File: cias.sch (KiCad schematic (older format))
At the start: 63 parts, among them CN13 KEYBOARD, CN6 SERIAL_DB25M, CN7 PARALLEL_DB25F, Q501 2N3904, Q502 2N3906, Q503 2N3906, Q711 2N3904, U38 MC1488, U39 MC1489, U42 NE555, U7 VIA_8520, U8 VIA_8520

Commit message: Almost all components positioned
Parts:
- C502: footprint (none) -> Raemixx500:C_Axial_L9.0mm_D3.2mm_P12.70mm
- E532, E533, E534, E535, E536, E537, E631, E632: footprint (none) -> Raemixx500:EMI_Filter_Short
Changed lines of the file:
@@
 F 0 "E532" H 7905 6900 50  0000 C CNN
 F 1 "150p" H 7855 6680 50  0000 C CNN
-F 2 "" V 8045 6710 50  0001 C CNN
+F 2 "Raemixx500:EMI_Filter_Short" V 8045 6710 50  0001 C CNN
 F 3 "http://www.murata.com/~/media/webrenewal/support/library/catalog/products/emc/emifil/c31e.ashx?la=en-gb" V 8045 6710 50  0001 C CNN
 	1    8045 6710
@@
 F 0 "E534" H 8430 7105 50  0000 C CNN
 F 1 "150p" H 8595 6880 50  0000 C CNN
-F 2 "" V 8430 6910 50  0001 C CNN
+F 2 "Raemixx500:EMI_Filter_Short" V 8430 6910 50  0001 C CNN
 F 3 "http://www.murata.com/~/media/webrenewal/support/library/catalog/products/emc/emifil/c31e.ashx?la=en-gb" V 8430 6910 50  0001 C CNN
 	1    8430 6910
@@
 F 0 "E533" H 7905 7300 50  0000 C CNN
 F 1 "470p" H 7855 7085 50  0000 C CNN
-F 2 "" V 8045 7110 50  0001 C CNN
+F 2 "Raemixx500:EMI_Filter_Short" V 8045 7110 50  0001 C CNN
 F 3 "http://www.murata.com/~/media/webrenewal/support/library/catalog/products/emc/emifil/c31e.ashx?la=en-gb" V 8045 7110 50  0001 C CNN
 	1    8045 7110
@@
 F 0 "E535" H 8430 7505 50  0000 C CNN
 F 1 "470p" H 8600 7280 50  0000 C CNN
-F 2 "" V 8430 7310 50  0001 C CNN
+F 2 "Raemixx500:EMI_Filter_Short" V 8430 7310 50  0001 C CNN
 F 3 "http://www.murata.com/~/media/webrenewal/support/library/catalog/products/emc/emifil/c31e.ashx?la=en-gb" V 8430 7310 50  0001 C CNN
 	1    8430 7310
@@
 F 0 "E536" H 7905 7700 50  0000 C CNN
 F 1 "470p" H 7860 7480 50  0000 C CNN
-F 2 "" V 8045 7510 50  0001 C CNN
+F 2 "Raemixx500:EMI_Filter_Short" V 8045 7510 50  0001 C CNN
 F 3 "http://www.murata.com/~/media/webrenewal/support/library/catalog/products/emc/emifil/c31e.ashx?la=en-gb" V 8045 7510 50  0001 C CNN
 	1    8045 7510
@@
 F 0 "E537" H 7905 8100 50  0000 C CNN
 F 1 "470p" H 7860 7880 50  0000 C CNN
-F 2 "" V 8045 7910 50  0001 C CNN
+F 2 "Raemixx500:EMI_Filter_Short" V 8045 7910 50  0001 C CNN
 F 3 "http://www.murata.com/~/media/webrenewal/support/library/catalog/products/emc/emifil/c31e.ashx?la=en-gb" V 8045 7910 50  0001 C CNN
 	1    8045 7910
@@
 F 0 "C502" V 8570 8410 50  0000 C CNN
 F 1 "330n" V 8415 8280 50  0000 C CNN
-F 2 "" H 8460 8410 50  0001 C CNN
+F 2 "Raemixx500:C_Axial_L9.0mm_D3.2mm_P12.70mm" H 8460 8410 50  0001 C CNN
 F 3 "~" H 8460 8410 50  0001 C CNN
 	1    8460 8410
@@
 F 0 "E632" H 14545 4275 50  0000 C CNN
 F 1 "100p" H 14350 4055 50  0000 C CNN
-F 2 "" V 14545 4085 50  0001 C CNN
+F 2 "Raemixx500:EMI_Filter_Short" V 14545 4085 50  0001 C CNN
 F 3 "http://www.murata.com/~/media/webrenewal/support/library/catalog/products/emc/emifil/c31e.ashx?la=en-gb" V 14545 4085 50  0001 C CNN
 	1    14545 4085
@@
 F 0 "E631" H 14545 4630 50  0000 C CNN
 F 1 "100p" H 14350 4410 50  0000 C CNN
-F 2 "" V 14545 4440 50  0001 C CNN
+F 2 "Raemixx500:EMI_Filter_Short" V 14545 4440 50  0001 C CNN
 F 3 "http://www.murata.com/~/media/webrenewal/support/library/catalog/products/emc/emifil/c31e.ashx?la=en-gb" V 14545 4440 50  0001 C CNN
 	1    14545 4440

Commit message: Work in progress
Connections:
- net GND: now also E531.2, E538.2
- net at E535.1: now also U39.4 (IN_B); no longer U39.13 (IN_D)
- net at E536.1: now also U39.10 (IN_C); no longer U39.4 (IN_B)
- net at E537.1: now also U39.13 (IN_D); no longer U39.10 (IN_C)
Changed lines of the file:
@@
 Wire Wire Line
 	8955 7410 8345 7410
-$Comp
-L emi_filter_lcl_small:EMI_Filter_LCL E536
-U 1 1 5EC70AF7
-P 8045 7510
-F 0 "E536" H 7905 7700 50  0000 C CNN
-F 1 "470p" H 7860 7480 50  0000 C CNN
-F 2 "Raemixx500:EMI_Filter_Short" V 8045 7510 50  0001 C CNN
-F 3 "http://www.murata.com/~/media/webrenewal/support/library/catalog/products/emc/emifil/c31e.ashx?la=en-gb" V 8045 7510 50  0001 C CNN
-	1    8045 7510
-	1    0    0    -1
-$EndComp
 Wire Wire Line
 	8955 7810 8345 7810
@@
 Wire Wire Line
 	5780 7060 6950 7060
-Wire Wire Line
-	5885 7210 8130 7210
 NoConn ~ 6090 7310
-Wire Wire Line
-	5885 7810 7745 7810
 NoConn ~ 5585 7710
 Wire Wire Line
@@
 Wire Wire Line
 	4980 5875 4065 5875
-Wire Wire Line
-	6390 7410 7745 7410
 Wire Wire Line
 	5890 7410 5080 7410
@@
 Wire Wire Line
 	13385 7495 13215 7495
+$Comp
+L emi_filter_lcl_small:EMI_Filter_LCL E536
+U 1 1 5EC70AF7
+P 8045 7510
+F 0 "E536" H 7905 7700 50  0000 C CNN
+F 1 "470p" H 7860 7480 50  0000 C CNN
+F 2 "Raemixx500:EMI_Filter_Short" V 8045 7510 50  0001 C CNN
+F 3 "http://www.murata.com/~/media/webrenewal/support/library/catalog/products/emc/emifil/c31e.ashx?la=en-gb" V 8045 7510 50  0001 C CNN
+	1    8045 7510
+	1    0    0    -1
+$EndComp
+Wire Wire Line
+	7040 7210 7040 7410
+Wire Wire Line
+	7040 7210 8130 7210
+Wire Wire Line
+	6820 7810 7745 7810
+Wire Wire Line
+	5885 7210 6820 7210
+Wire Wire Line
+	6820 7210 6820 7810
+Wire Wire Line
+	5885 7810 6545 7810
+Wire Wire Line
+	6390 7410 7040 7410
+Wire Wire Line
+	7745 7410 7235 7410
+Wire Wire Line
+	7235 7410 7235 7585
+Wire Wire Line
+	7235 7585 6545 7585
+Wire Wire Line
+	6545 7585 6545 7810
+$Comp
+L power:GND #PWR?
+U 1 1 5DBE430E
+P 10690 8395
+F 0 "#PWR?" H 10690 8145 50  0001 C CNN
+F 1 "GND" H 10695 8222 50  0000 C CNN
+F 2 "" H 10690 8395 50  0001 C CNN
+F 3 "" H 10690 8395 50  0001 C CNN
+	1    10690 8395
+	1    0    0    -1
+$EndComp
+Wire Wire Line
+	10690 8395 10690 8310
+Connection ~ 10690 8310
 Wire Bus Line
 	1785 3110 1785 6275

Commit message: Work in progress
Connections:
- net ~OVL renamed OVL
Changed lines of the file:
@@
 ~LED
 Text GLabel 4385 3310 2    50   Output ~ 0
-~OVL
+OVL
 $Comp
 L power:VCC #PWR0162
@@
 	6545 7585 6545 7810
 $Comp
-L power:GND #PWR?
+L power:GND #PWR0268
 U 1 1 5DBE430E
 P 10690 8395
-F 0 "#PWR?" H 10690 8145 50  0001 C CNN
+F 0 "#PWR0268" H 10690 8145 50  0001 C CNN
 F 1 "GND" H 10695 8222 50  0000 C CNN
 F 2 "" H 10690 8395 50  0001 C CNN

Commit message: Work in progress
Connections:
- net FIRE0 renamed ~FIRE0
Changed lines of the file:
@@
 ~FIRE1
 Text GLabel 4310 2710 2    50   Input ~ 0
-FIRE0
+~FIRE0
 Text GLabel 4580 2810 2    50   Input ~ 0
 ~RDY

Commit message: Work in progress
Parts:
- removed E501, E502, E503: 47, Raemixx500:EMI_Filter_Longer, symbol Device:R
- added E501, E502, E503: 47 1/2W, Raemixx500:EMI_Filter_Longer, symbol emi_filter_lcl_small:EMI_Filter_LCL
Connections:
- net +12V: now also E502.1
- net +v: now also E502.3
- net -12V: now also E503.1
- net -v: now also E503.3
- net GND: now also E501.2, E502.2, E503.2
- net VCC: now also E501.1
- net ~auto: now also E501.3
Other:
- note removed: "1/2W"
- moved on the sheet: C502
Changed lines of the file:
@@
 Sheet 6 14
 Title "Rämixx500"
-Date "2019-05-08"
+Date "2019-05-11"
 Rev "1git"
 Comp "SukkoPera"
@@
 Wire Wire Line
 	9555 1490 9805 1490
-$Comp
-L power:VCC #PWR0160
-U 1 1 5E872212
-P 10215 1425
-F 0 "#PWR0160" H 10215 1275 50  0001 C CNN
-F 1 "VCC" H 10232 1598 50  0000 C CNN
-F 2 "" H 10215 1425 50  0001 C CNN
-F 3 "" H 10215 1425 50  0001 C CNN
-	1    10215 1425
-	1    0    0    -1
-$EndComp
-Wire Wire Line
-	10215 1425 10215 1490
-Wire Wire Line
-	10215 1490 10105 1490
-$Comp
-L Device:R E501
-U 1 1 5E870508
-P 9955 1490
-F 0 "E501" V 9870 1490 50  0000 C CNN
-F 1 "47" V 9955 1490 50  0000 C CNN
-F 2 "Raemixx500:EMI_Filter_Longer" V 9885 1490 50  0001 C CNN
-F 3 "~" H 9955 1490 50  0001 C CNN
-	1    9955 1490
-	0    1    1    0
-$EndComp
-Text Notes 9845 1345 0    50   ~ 0
-1/2W
 Text Label 9590 1490 0    50   ~ 0
 ~auto
@@
 	9555 1890 9650 1890
 Wire Wire Line
-	10250 1890 10390 1890
-Text GLabel 10390 1890 2    50   Input ~ 0
+	10250 1890 10495 1890
+Text GLabel 10495 1890 2    50   Input ~ 0
 ~IORESET
 Connection ~ 9950 2090
@@
 	8780 9235 8780 9115
 Wire Wire Line
-	8780 7610 8780 9115
-Wire Wire Line
 	8430 7610 8780 7610
 Wire Wire Line
@@
 fg
 NoConn ~ 8560 6410
-$Comp
-L Device:R E503
-U 1 1 5EDCA2BC
-P 8505 8210
-F 0 "E503" V 8420 8210 50  0000 C CNN
-F 1 "47" V 8505 8210 50  0000 C CNN
-F 2 "Raemixx500:EMI_Filter_Longer" V 8435 8210 50  0001 C CNN
-F 3 "~" H 8505 8210 50  0001 C CNN
-	1    8505 8210
-	0    1    1    0
-$EndComp
-Text Notes 8180 8300 0    50   ~ 0
-1/2W
-$Comp
-L Device:R E502
-U 1 1 5EDDB02D
-P 8505 8010
-F 0 "E502" V 8420 8010 50  0000 C CNN
-F 1 "47" V 8505 8010 50  0000 C CNN
-F 2 "Raemixx500:EMI_Filter_Longer" V 8435 8010 50  0001 C CNN
-F 3 "~" H 8505 8010 50  0001 C CNN
-	1    8505 8010
-	0    1    1    0
-$EndComp
-Text Notes 8185 8095 0    50   ~ 0
-1/2W
-Wire Wire Line
-	8655 8010 8955 8010
-Wire Wire Line
-	8655 8210 8955 8210
 Wire Wire Line
 	7495 8010 7495 7990
 Wire Wire Line
-	7495 8010 8355 8010
+	7495 8010 8130 8010
 $Comp
 L power:+12V #PWR0164
@@
 	7495 8210 7495 8170
 Wire Wire Line
-	7495 8210 8355 8210
+	7495 8210 7745 8210
 Wire Wire Line
 	8560 8610 8955 8610
@@
 Text GLabel 10355 7310 2    50   Output ~ 0
 AUDIN
-Wire Wire Line
-	8955 8410 8560 8410
 $Comp
 L Device:C_Small C502
 U 1 1 5EEC226F
-P 8460 8410
-F 0 "C502" V 8570 8410 50  0000 C CNN
-F 1 "330n" V 8415 8280 50  0000 C CNN
-F 2 "Raemixx500:C_Axial_L9.0mm_D3.2mm_P12.70mm" H 8460 8410 50  0001 C CNN
-F 3 "~" H 8460 8410 50  0001 C CNN
-	1    8460 8410
+P 7935 8610
+F 0 "C502" V 8045 8610 50  0000 C CNN
+F 1 "330n" V 7890 8480 50  0000 C CNN
+F 2 "Raemixx500:C_Axial_L9.0mm_D3.2mm_P12.70mm" H 7935 8610 50  0001 C CNN
+F 3 "~" H 7935 8610 50  0001 C CNN
+	1    7935 8610
 	0    1    1    0
 $EndComp
 Wire Wire Line
-	8360 8410 8155 8410
-Text GLabel 8155 8410 0    50   Input ~ 0
+	7835 8610 7390 8610
+Text GLabel 7390 8610 0    50   Input ~ 0
 AUDOUT
 Wire Wire Line
@@
 Wire Wire Line
 	5175 5675 4065 5675
-Text Notes 7240 8735 2    315  ~ 0
+Text Notes 7270 9190 2    315  ~ 0
 RS232
 Text Notes 8525 1090 2    315  ~ 0
@@
 Connection ~ 7615 8080
 Wire Wire Line
-	7615 8080 7615 9115
+	7615 8080 7615 8480
 $Comp
 L Device:R R713
@@
 	10690 8395 10690 8310
 Connection ~ 10690 8310
+$Comp
+L emi_filter_lcl_small:EMI_Filter_LCL E502
+U 1 1 5E0EA71F
+P 8430 8110
+F 0 "E502" H 8430 8305 50  0000 C CNN
+F 1 "47 1/2W" H 8600 8080 50  0000 C CNN
+F 2 "Raemixx500:EMI_Filter_Longer" V 8430 8110 50  0001 C CNN
+F 3 "http://www.murata.com/~/media/webrenewal/support/library/catalog/products/emc/emifil/c31e.ashx?la=en-gb" V 8430 8110 50  0001 C CNN
+	1    8430 8110
+	1    0    0    -1
+$EndComp
+$Comp
+L emi_filter_lcl_small:EMI_Filter_LCL E503
+U 1 1 5E0EA729
+P 8045 8310
+F 0 "E503" H 7905 8500 50  0000 C CNN
+F 1 "47 1/2W" H 7800 8280 50  0000 C CNN
+F 2 "Raemixx500:EMI_Filter_Longer" V 8045 8310 50  0001 C CNN
+F 3 "http://www.murata.com/~/media/webrenewal/support/library/catalog/products/emc/emifil/c31e.ashx?la=en-gb" V 8045 8310 50  0001 C CNN
+	1    8045 8310
+	1    0    0    -1
+$EndComp
+Wire Wire Line
+	8730 8010 8955 8010
+Wire Wire Line
+	8345 8210 8955 8210
+Wire Wire Line
+	8780 7610 8780 8270
+Wire Wire Line
+	8430 8160 8430 8270
+Wire Wire Line
+	8430 8270 8780 8270
+Connection ~ 8780 8270
+Wire Wire Line
+	8780 8270 8780 9115
+Wire Wire Line
+	8045 8360 8045 8480
+Wire Wire Line
+	8045 8480 7615 8480
+Connection ~ 7615 8480
+Wire Wire Line
+	7615 8480 7615 9115
+Wire Wire Line
+	8035 8610 8430 8610
+Wire Wire Line
+	8430 8610 8430 8410
+Wire Wire Line
+	8430 8410 8955 8410
+$Comp
+L power:VCC #PWR0160
+U 1 1 5E872212
+P 10515 1425
+F 0 "#PWR0160" H 10515 1275 50  0001 C CNN
+F 1 "VCC" H 10532 1598 50  0000 C CNN
+F 2 "" H 10515 1425 50  0001 C CNN
+F 3 "" H 10515 1425 50  0001 C CNN
+	1    10515 1425
+	1    0    0    -1
+$EndComp
+Wire Wire Line
+	10515 1425 10515 1490
+Wire Wire Line
+	10515 1490 10405 1490
+$Comp
+L emi_filter_lcl_small:EMI_Filter_LCL E501
+U 1 1 5E3D78DB
+P 10105 1590
+F 0 "E501" H 10105 1785 50  0000 C CNN
+F 1 "47 1/2W" H 9870 1560 50  0000 C CNN
+F 2 "Raemixx500:EMI_Filter_Longer" V 10105 1590 50  0001 C CNN
+F 3 "http://www.murata.com/~/media/webrenewal/support/library/catalog/products/emc/emifil/c31e.ashx?la=en-gb" V 10105 1590 50  0001 C CNN
+	1    10105 1590
+	-1   0    0    -1
+$EndComp
+Wire Wire Line
+	10105 1640 10105 1720
+Wire Wire Line
+	10105 1720 10325 1720
+Wire Wire Line
+	10325 1720 10325 2290
+Wire Wire Line
+	10325 2290 9950 2290
 Wire Bus Line
 	1785 3110 1785 6275

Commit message: Almost there :)
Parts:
- CN7: footprint w_conn_d-sub:DB_25M -> Raemixx500:DB_25F
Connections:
- net d0: no longer U8.33 (D0)
- net d1: no longer U8.32 (D1)
- net d2: no longer U8.31 (D2)
- net d3: no longer U8.30 (D3)
- net d4: no longer U8.29 (D4)
- net d5: no longer U8.28 (D5)
- net d6: no longer U8.27 (D6)
- net d7: no longer U8.26 (D7)
- new net d10: U8.31 (D2)
- new net d11: U8.30 (D3)
- new net d12: U8.29 (D4)
- new net d13: U8.28 (D5)
- new net d14: U8.27 (D6)
- new net d15: U8.26 (D7)
- new net d8: U8.33 (D0)
- new net d9: U8.32 (D1)
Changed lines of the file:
@@
 Sheet 6 14
 Title "Rämixx500"
-Date "2019-05-11"
+Date "2019-06-23"
 Rev "1git"
 Comp "SukkoPera"
@@
 ~INT6
 Text Label 2415 5225 0    50   ~ 0
-d7
+d15
 Text Label 2415 5325 0    50   ~ 0
-d6
+d14
 Text Label 2415 5425 0    50   ~ 0
-d5
+d13
 Text Label 2415 5525 0    50   ~ 0
-d4
+d12
 Text Label 2415 5625 0    50   ~ 0
-d3
+d11
 Text Label 2415 5725 0    50   ~ 0
-d2
+d10
 Text Label 2415 5825 0    50   ~ 0
-d1
+d9
 Text Label 2415 5925 0    50   ~ 0
-d0
+d8
 Text Label 2415 6075 0    50   ~ 0
 a11
@@
 F 0 "CN7" H 9255 4082 50  0000 C CNN
 F 1 "PARALLEL_DB25F" H 9255 3991 50  0000 C CNN
-F 2 "w_conn_d-sub:DB_25M" H 9255 2590 50  0001 C CNN
+F 2 "Raemixx500:DB_25F" H 9255 2590 50  0001 C CNN
 F 3 " ~" H 9255 2590 50  0001 C CNN
 	1    9255 2590

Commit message: Fix shielding of D-Sub connectors
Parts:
- CN6: footprint w_conn_d-sub:DB_25M -> Raemixx500:DB_25M
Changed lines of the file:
@@
 F 0 "CN6" H 9255 6035 50  0000 C CNN
 F 1 "SERIAL_DB25M" H 9255 6135 50  0000 C CNN
-F 2 "w_conn_d-sub:DB_25M" H 9255 7610 50  0001 C CNN
+F 2 "Raemixx500:DB_25M" H 9255 7610 50  0001 C CNN
 F 3 " ~" H 9255 7610 50  0001 C CNN
 	1    9255 7610

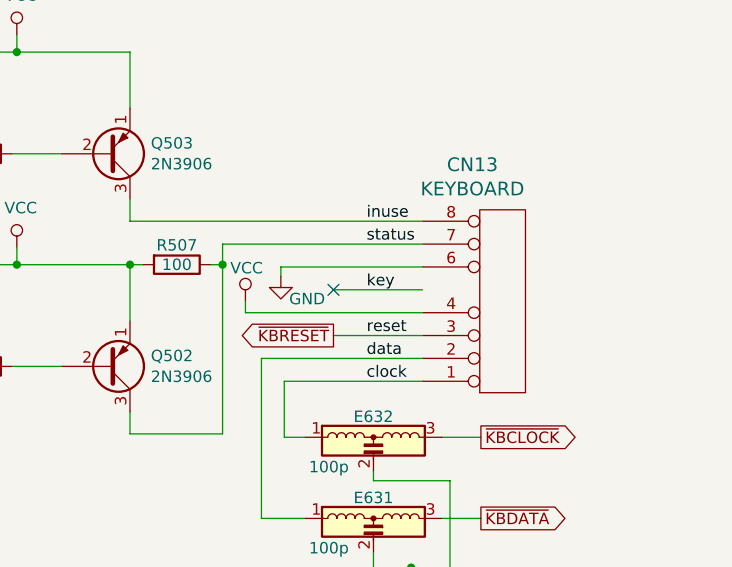
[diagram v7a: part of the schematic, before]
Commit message: Fix keyboard connector key pin
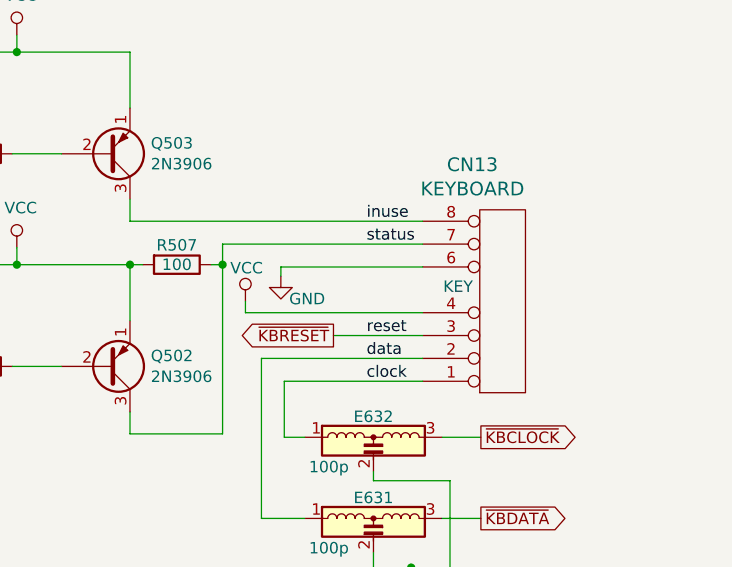
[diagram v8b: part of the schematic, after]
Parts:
- CN13: footprint Connector_PinHeader_2.54mm:PinHeader_1x08_P2.54mm_Vertical -> Raemixx500:Keyboard_Connector
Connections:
- no-connect marks 21 -> 20
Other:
- note added: "KEY"
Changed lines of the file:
@@
 F 0 "CN13" H 14978 2793 60  0000 C CNN
 F 1 "KEYBOARD" H 14978 2899 60  0000 C CNN
-F 2 "Connector_PinHeader_2.54mm:PinHeader_1x08_P2.54mm_Vertical" H 15110 3390 50  0001 C CNN
+F 2 "Raemixx500:Keyboard_Connector" H 15110 3390 50  0001 C CNN
 F 3 "" H 15110 3390 50  0001 C CNN
 	1    15110 3390
@@
 $EndComp
 Wire Wire Line
-	14760 3340 14370 3340
-Wire Wire Line
 	14760 3540 14370 3540
-NoConn ~ 14370 3340
-Text Label 14515 3340 0    50   ~ 0
-key
 Wire Wire Line
 	13480 2945 13480 3040
@@
 Wire Bus Line
 	1950 2260 1950 5825
+Text Notes 14850 3365 0    50   ~ 0
+KEY
 $EndSCHEMATC
